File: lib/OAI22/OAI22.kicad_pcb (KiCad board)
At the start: 2 copper layers, 8 parts

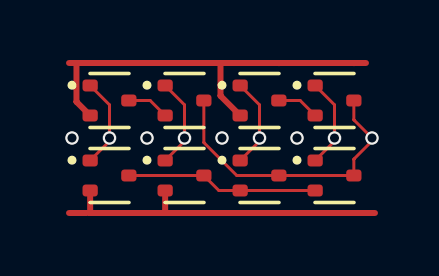
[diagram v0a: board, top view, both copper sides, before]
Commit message: High-density layout with pitch of 1.1mm, which gains 23% !!
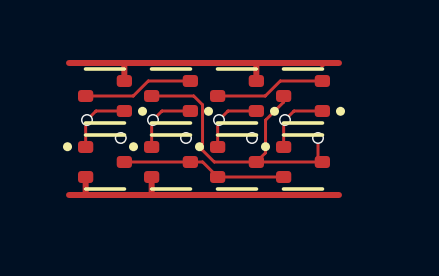
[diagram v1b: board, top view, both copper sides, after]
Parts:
- moved N4 1.14 mm to (7.70, 3.30)
- moved P4 1.06 mm to (7.70, 1.10), turned to 180 degrees
- moved N3 0.87 mm to (5.50, 3.30)
- moved P3 0.76 mm to (5.50, 1.10), turned to 180 degrees
- moved N2 0.64 mm to (3.30, 3.30)
- moved N1 0.47 mm to (1.10, 3.30)
- moved P2 0.47 mm to (3.30, 1.10), turned to 180 degrees
- moved P1 0.21 mm to (1.10, 1.10), turned to 180 degrees
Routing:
- net VDD: track 14.1 -> 10.3 mm
- net intA: track 1.42 -> 3.70 mm
- net intB: track 1.42 -> 3.70 mm
- net GND: track 11.6 -> 10.2 mm
- net Y: track 9.86 -> 10.9 mm
- net intN: track 6.42 -> 5.52 mm
- net A2: track 3.03 -> 2.29 mm
- net B1: track 3.03 -> 2.29 mm
- net A1: track 3.03 -> 2.29 mm
- net B2: track 3.03 -> 2.29 mm
- net (no net): vias 4 -> 3

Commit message: All cells now use 1mm*4mm grid rather than 1.1mm*4.4mm
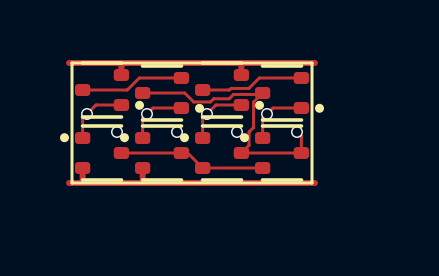
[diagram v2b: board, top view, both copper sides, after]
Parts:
- moved N4 0.76 mm to (7.00, 3.00)
- moved P4 0.71 mm to (7.00, 1.00)
- moved N3 0.58 mm to (5.00, 3.00)
- moved P3 0.54 mm to (5.00, 0.90)
- moved N2 0.42 mm to (3.00, 3.00)
- moved N1 0.32 mm to (1.00, 3.00)
- moved P2 0.32 mm to (3.00, 1.00)
- moved P1 0.22 mm to (1.00, 0.90)
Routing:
- net Y: track 10.9 -> 9.30 mm
- net VDD: track 10.3 -> 9.06 mm
- net GND: track 10.2 -> 9.25 mm
- net intN: track 5.52 -> 4.92 mm

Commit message: Make the pads of my SOT523 footprint very slightly smaller, which is enough to route all the cells and leave the mosfets exactly on the grid
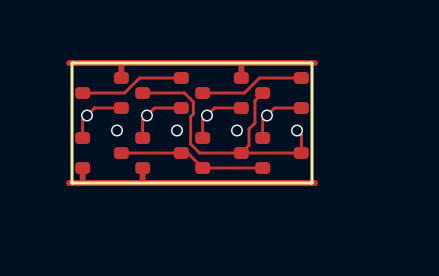
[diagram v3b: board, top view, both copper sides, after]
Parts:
- N1, N2, N3, N4, P1, P2, P3, P4: footprint Package_TO_SOT_SMD:SOT-523 -> RV523:SOT523
- moved P1 0.10 mm to (1.00, 1.00)
- moved P3 0.10 mm to (5.00, 1.00)
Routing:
- net Y: track 9.30 -> 10.2 mm

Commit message: Propagate MOSFET values to the cells' PCBs
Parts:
- N1, N2, N3, N4: value (none) -> NMOS
- P1, P2, P3, P4: value (none) -> PMOS
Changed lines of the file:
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@@
 			)
 		)
-		(property "Value" ""
+		(property "Value" "NMOS"
 			(at 0 0 0)
 			(layer "F.Fab")
@@
 			)
 		)
-		(property "Value" ""
+		(property "Value" "PMOS"
 			(at 0 0 180)
 			(layer "F.Fab")
@@
 			)
 		)
-		(property "Value" ""
+		(property "Value" "PMOS"
 			(at 0 0 180)
 			(layer "F.Fab")
@@
 			)
 		)
-		(property "Value" ""
+		(property "Value" "PMOS"
 			(at 0 0 180)
 			(layer "F.Fab")
@@
 			)
 		)
-		(property "Value" ""
+		(property "Value" "PMOS"
 			(at 0 0 180)
 			(layer "F.Fab")
@@
 			)
 		)
-		(property "Value" ""
+		(property "Value" "NMOS"
 			(at 0 0 0)
 			(layer "F.Fab")
@@
 			)
 		)
-		(property "Value" ""
+		(property "Value" "NMOS"
 			(at 0 0 0)
 			(layer "F.Fab")
@@
 			)
 		)
-		(property "Value" ""
+		(property "Value" "NMOS"
 			(at 0 0 0)
 			(layer "F.Fab")
